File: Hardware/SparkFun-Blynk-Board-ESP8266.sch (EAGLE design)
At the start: 104 parts, among them IC1 LMV358, Q1 2.5A/30V, Q2 MMBT2222A, Q3 MMBT2222A, U1 MCP73831, U2 ESP8266, U3 AP2112K-3.3V, U4 FT231XS-U, U5 W25Q32FVSS, U6 SI7021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

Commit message: Moving some silk. Updating version number to v10.
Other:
- note added: "v10"
- note removed: "v02"
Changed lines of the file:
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@@
 <grid distance="0.1" unitdist="inch" unit="inch" style="lines" multiple="1" display="no" altdistance="0.01" altunitdist="inch" altunit="inch"/>
 <layers>
-<layer number="1" name="Top" color="4" fill="1" visible="yes" active="no"/>
-<layer number="2" name="Route2" color="1" fill="3" visible="yes" active="no"/>
-<layer number="3" name="Route3" color="4" fill="3" visible="yes" active="no"/>
-<layer number="4" name="Route4" color="1" fill="4" visible="yes" active="no"/>
-<layer number="5" name="Route5" color="4" fill="4" visible="yes" active="no"/>
-<layer number="6" name="Route6" color="1" fill="8" visible="yes" active="no"/>
-<layer number="7" name="Route7" color="4" fill="8" visible="yes" active="no"/>
-<layer number="8" name="Route8" color="1" fill="2" visible="yes" active="no"/>
-<layer number="9" name="Route9" color="4" fill="2" visible="yes" active="no"/>
-<layer number="10" name="Route10" color="1" fill="7" visible="yes" active="no"/>
-<layer number="11" name="Route11" color="4" fill="7" visible="yes" active="no"/>
-<layer number="12" name="Route12" color="1" fill="5" visible="yes" active="no"/>
-<layer number="13" name="Route13" color="4" fill="5" visible="yes" active="no"/>
-<layer number="14" name="Route14" color="1" fill="6" visible="yes" active="no"/>
-<layer number="15" name="Route15" color="4" fill="6" visible="yes" active="no"/>
-<layer number="16" name="Bottom" color="1" fill="1" visible="yes" active="no"/>
-<layer number="17" name="Pads" color="2" fill="1" visible="yes" active="no"/>
-<layer number="18" name="Vias" color="2" fill="1" visible="yes" active="no"/>
-<layer number="19" name="Unrouted" color="6" fill="1" visible="yes" active="no"/>
-<layer number="20" name="Dimension" color="15" fill="1" visible="yes" active="no"/>
-<layer number="21" name="tPlace" color="16" fill="1" visible="yes" active="no"/>
-<layer number="22" name="bPlace" color="14" fill="1" visible="yes" active="no"/>
-<layer number="23" name="tOrigins" color="15" fill="1" visible="yes" active="no"/>
-<layer number="24" name="bOrigins" color="15" fill="1" visible="yes" active="no"/>
-<layer number="25" name="tNames" color="7" fill="1" visible="yes" active="no"/>
-<layer number="26" name="bNames" color="7" fill="1" visible="yes" active="no"/>
-<layer number="27" name="tValues" color="7" fill="1" visible="yes" active="no"/>
-<layer number="28" name="bValues" color="7" fill="1" visible="yes" active="no"/>
+<layer number="1" name="Top" color="4" fill="1" visible="no" active="no"/>
+<layer number="2" name="Route2" color="1" fill="3" visible="no" active="no"/>
+<layer number="3" name="Route3" color="4" fill="3" visible="no" active="no"/>
+<layer number="4" name="Route4" color="1" fill="4" visible="no" active="no"/>
+<layer number="5" name="Route5" color="4" fill="4" visible="no" active="no"/>
+<layer number="6" name="Route6" color="1" fill="8" visible="no" active="no"/>
+<layer number="7" name="Route7" color="4" fill="8" visible="no" active="no"/>
+<layer number="8" name="Route8" color="1" fill="2" visible="no" active="no"/>
+<layer number="9" name="Route9" color="4" fill="2" visible="no" active="no"/>
+<layer number="10" name="Route10" color="1" fill="7" visible="no" active="no"/>
+<layer number="11" name="Route11" color="4" fill="7" visible="no" active="no"/>
+<layer number="12" name="Route12" color="1" fill="5" visible="no" active="no"/>
+<layer number="13" name="Route13" color="4" fill="5" visible="no" active="no"/>
+<layer number="14" name="Route14" color="1" fill="6" visible="no" active="no"/>
+<layer number="15" name="Route15" color="4" fill="6" visible="no" active="no"/>
+<layer number="16" name="Bottom" color="1" fill="1" visible="no" active="no"/>
+<layer number="17" name="Pads" color="2" fill="1" visible="no" active="no"/>
+<layer number="18" name="Vias" color="2" fill="1" visible="no" active="no"/>
+<layer number="19" name="Unrouted" color="6" fill="1" visible="no" active="no"/>
+<layer number="20" name="Dimension" color="15" fill="1" visible="no" active="no"/>
+<layer number="21" name="tPlace" color="16" fill="1" visible="no" active="no"/>
+<layer number="22" name="bPlace" color="14" fill="1" visible="no" active="no"/>
+<layer number="23" name="tOrigins" color="15" fill="1" visible="no" active="no"/>
+<layer number="24" name="bOrigins" color="15" fill="1" visible="no" active="no"/>
+<layer number="25" name="tNames" color="7" fill="1" visible="no" active="no"/>
+<layer number="26" name="bNames" color="7" fill="1" visible="no" active="no"/>
+<layer number="27" name="tValues" color="7" fill="1" visible="no" active="no"/>
+<layer number="28" name="bValues" color="7" fill="1" visible="no" active="no"/>
 <layer number="29" name="tStop" color="7" fill="3" visible="no" active="no"/>
 <layer number="30" name="bStop" color="7" fill="6" visible="no" active="no"/>
@@
 <layer number="35" name="tGlue" color="7" fill="4" visible="no" active="no"/>
 <layer number="36" name="bGlue" color="7" fill="5" visible="no" active="no"/>
-<layer number="37" name="tTest" color="7" fill="1" visible="yes" active="no"/>
-<layer number="38" name="bTest" color="7" fill="1" visible="yes" active="no"/>
+<layer number="37" name="tTest" color="7" fill="1" visible="no" active="no"/>
+<layer number="38" name="bTest" color="7" fill="1" visible="no" active="no"/>
 <layer number="39" name="tKeepout" color="4" fill="11" visible="no" active="no"/>
 <layer number="40" name="bKeepout" color="1" fill="11" visible="no" active="no"/>
@@
 <layer number="44" name="Drills" color="7" fill="1" visible="no" active="no"/>
 <layer number="45" name="Holes" color="7" fill="1" visible="no" active="no"/>
-<layer number="46" name="Milling" color="3" fill="1" visible="yes" active="no"/>
-<layer number="47" name="Measures" color="7" fill="1" visible="yes" active="no"/>
-<layer number="48" name="Document" color="7" fill="1" visible="yes" active="no"/>
-<layer number="49" name="Reference" color="7" fill="1" visible="yes" active="no"/>
-<layer number="50" name="dxf" color="7" fill="1" visible="yes" active="no"/>
-<layer number="51" name="tDocu" color="6" fill="1" visible="yes" active="no"/>
-<layer number="52" name="bDocu" color="7" fill="1" visible="yes" active="no"/>
-<layer number="53" name="tGND_GNDA" color="7" fill="9" visible="yes" active="no"/>
-<layer number="54" name="bGND_GNDA" color="1" fill="9" visible="yes" active="no"/>
-<layer number="56" name="wert" color="7" fill="1" visible="yes" active="no"/>
-<layer number="57" name="tCAD" color="7" fill="1" visible="yes" active="no"/>
-<layer number="59" name="tCarbon" color="7" fill="1" visible="yes" active="no"/>
-<layer number="60" name="bCarbon" color="7" fill="1" visible="yes" active="no"/>
+<layer number="46" name="Milling" color="3" fill="1" visible="no" active="no"/>
+<layer number="47" name="Measures" color="7" fill="1" visible="no" active="no"/>
+<layer number="48" name="Document" color="7" fill="1" visible="no" active="no"/>
+<layer number="49" name="Reference" color="7" fill="1" visible="no" active="no"/>
+<layer number="50" name="dxf" color="7" fill="1" visible="no" active="no"/>
+<layer number="51" name="tDocu" color="6" fill="1" visible="no" active="no"/>
+<layer number="52" name="bDocu" color="7" fill="1" visible="no" active="no"/>
+<layer number="53" name="tGND_GNDA" color="7" fill="9" visible="no" active="no"/>
+<layer number="54" name="bGND_GNDA" color="1" fill="9" visible="no" active="no"/>
+<layer number="56" name="wert" color="7" fill="1" visible="no" active="no"/>
+<layer number="57" name="tCAD" color="7" fill="1" visible="no" active="no"/>
+<layer number="59" name="tCarbon" color="7" fill="1" visible="no" active="no"/>
+<layer number="60" name="bCarbon" color="7" fill="1" visible="no" active="no"/>
 <layer number="90" name="Modules" color="5" fill="1" visible="yes" active="yes"/>
 <layer number="91" name="Nets" color="2" fill="1" visible="yes" active="yes"/>
@@
 lots of power.)</text>
 <text x="355.346" y="11.43" size="2.54" layer="94" rot="MR180" align="top-left">Jim Lindblom</text>
-<text x="421.64" y="10.16" size="2.54" layer="94" align="top-left">v02</text>
+<text x="421.64" y="10.16" size="2.54" layer="94" align="top-left">v10</text>
 <text x="332.486" y="6.35" size="2.032" layer="97" rot="MR180" align="top-left">Auto-reset circuit based on NodeMCU Dev Kit</text>
 <text x="386.08" y="76.2" size="1.524" layer="97">GPIO2 pulled up in I2C section</text>

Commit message: Updating PROD_ID on JP29.
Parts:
- JP29: PROD_ID TBD -> (none)
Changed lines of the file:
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@@
 <part name="SUPPLY1" library="SparkFun-Aesthetics" deviceset="VCC" device=""/>
 <part name="GND6" library="SparkFun-Aesthetics" deviceset="GND" device=""/>
-<part name="JP29" library="SparkFun-Connectors" deviceset="M04" device="JST-PTH-VERT">
-<attribute name="PROD_ID" value="TBD"/>
-</part>
+<part name="JP29" library="SparkFun-Connectors" deviceset="M04" device="JST-PTH-VERT"/>
 <part name="SUPPLY3" library="SparkFun-Aesthetics" deviceset="VCC" device=""/>
 <part name="GND42" library="SparkFun-Aesthetics" deviceset="GND" device=""/>
@@
 <instance part="JP6" gate="G$1" x="165.1" y="81.28"/>
 <instance part="D4" gate="G$1" x="121.92" y="160.02" rot="MR0"/>
-<instance part="JP14" gate="G$1" x="149.86" y="160.02" smashed="yes" rot="R180">
+<instance part="JP14" gate="J$1" x="149.86" y="160.02" smashed="yes" rot="R180">
 <attribute name="VALUE" x="152.4" y="167.64" size="1.778" layer="96" rot="R180"/>
 <attribute name="NAME" x="152.4" y="154.178" size="1.778" layer="95" rot="R180"/>
@@
 <pinref part="GND25" gate="1" pin="GND"/>
 <wire x1="139.7" y1="160.02" x2="139.7" y2="154.94" width="0.1524" layer="91"/>
-<pinref part="JP14" gate="G$1" pin="2"/>
+<pinref part="JP14" gate="J$1" pin="2"/>
 <wire x1="142.24" y1="160.02" x2="139.7" y2="160.02" width="0.1524" layer="91"/>
 </segment>
@@
 <segment>
 <pinref part="D4" gate="G$1" pin="DOUT"/>
-<pinref part="JP14" gate="G$1" pin="3"/>
+<pinref part="JP14" gate="J$1" pin="3"/>
 <wire x1="127" y1="157.48" x2="142.24" y2="157.48" width="0.1524" layer="91"/>
 </segment>
@@
 <net name="N$19" class="0">
 <segment>
-<pinref part="JP14" gate="G$1" pin="1"/>
+<pinref part="JP14" gate="J$1" pin="1"/>
 <wire x1="142.24" y1="162.56" x2="139.7" y2="162.56" width="0.1524" layer="91"/>
 <pinref part="SJ3" gate="G$1" pin="1"/>

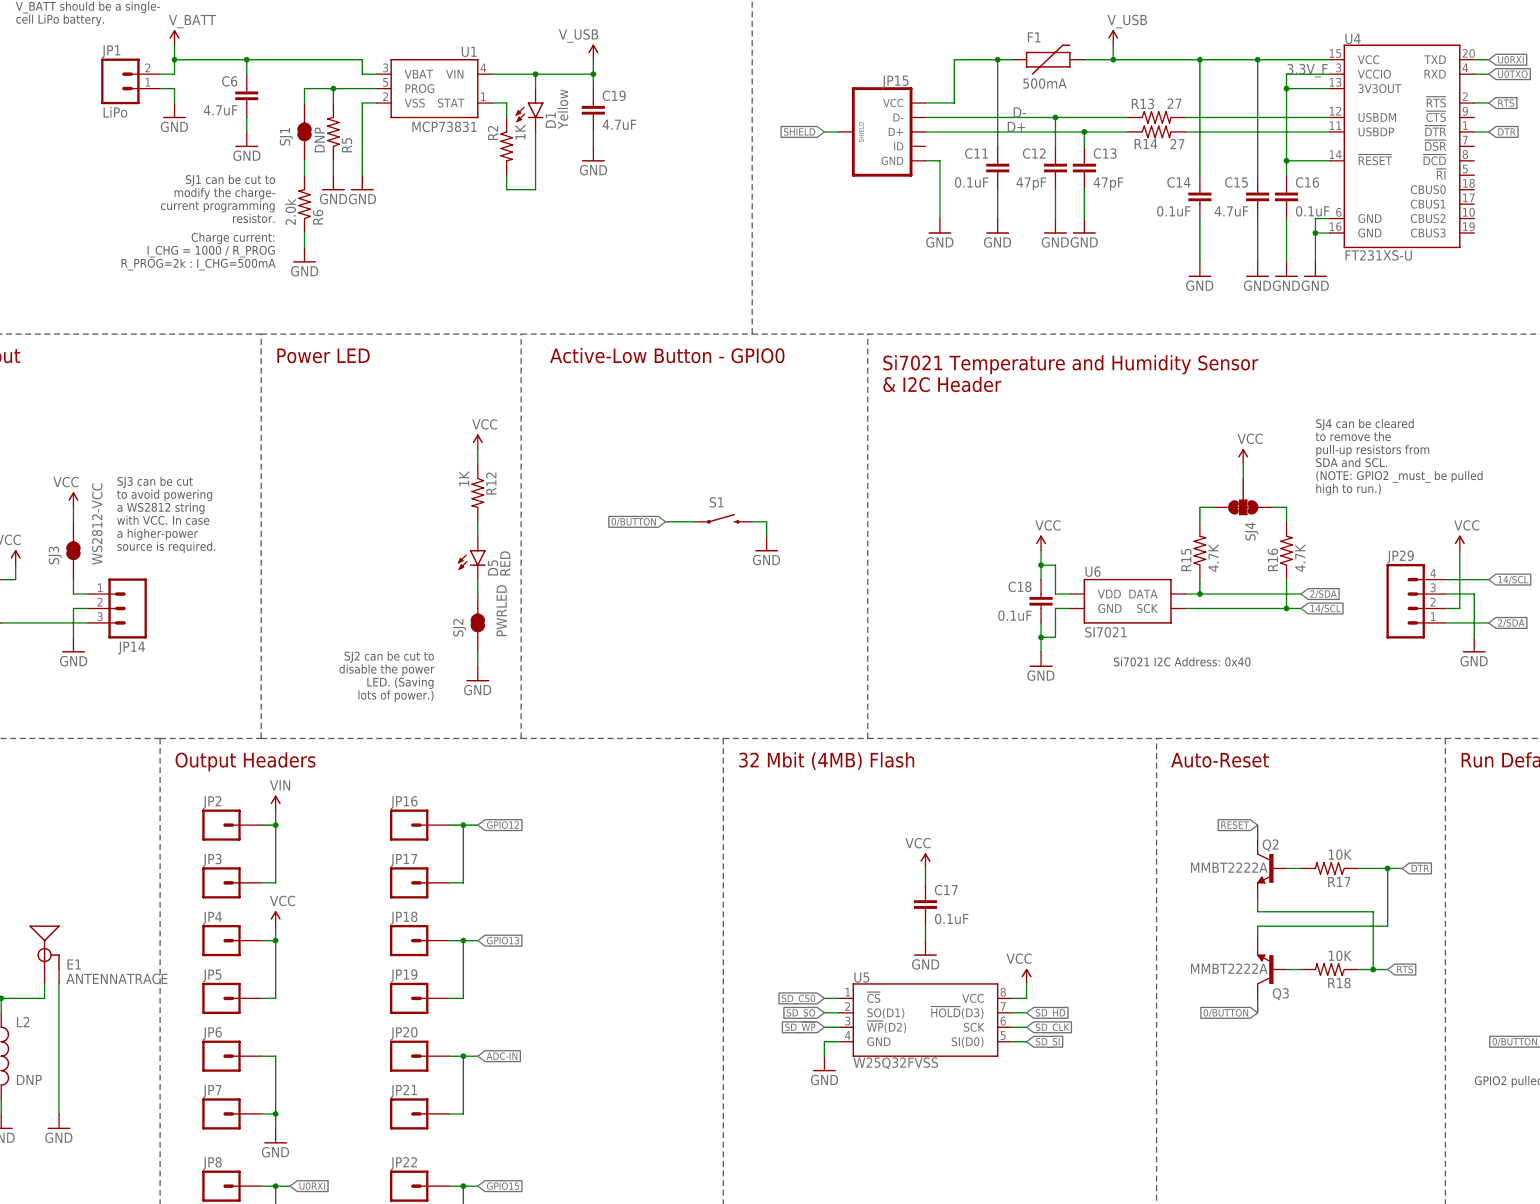
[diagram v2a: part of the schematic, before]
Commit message: Adding values to all parts
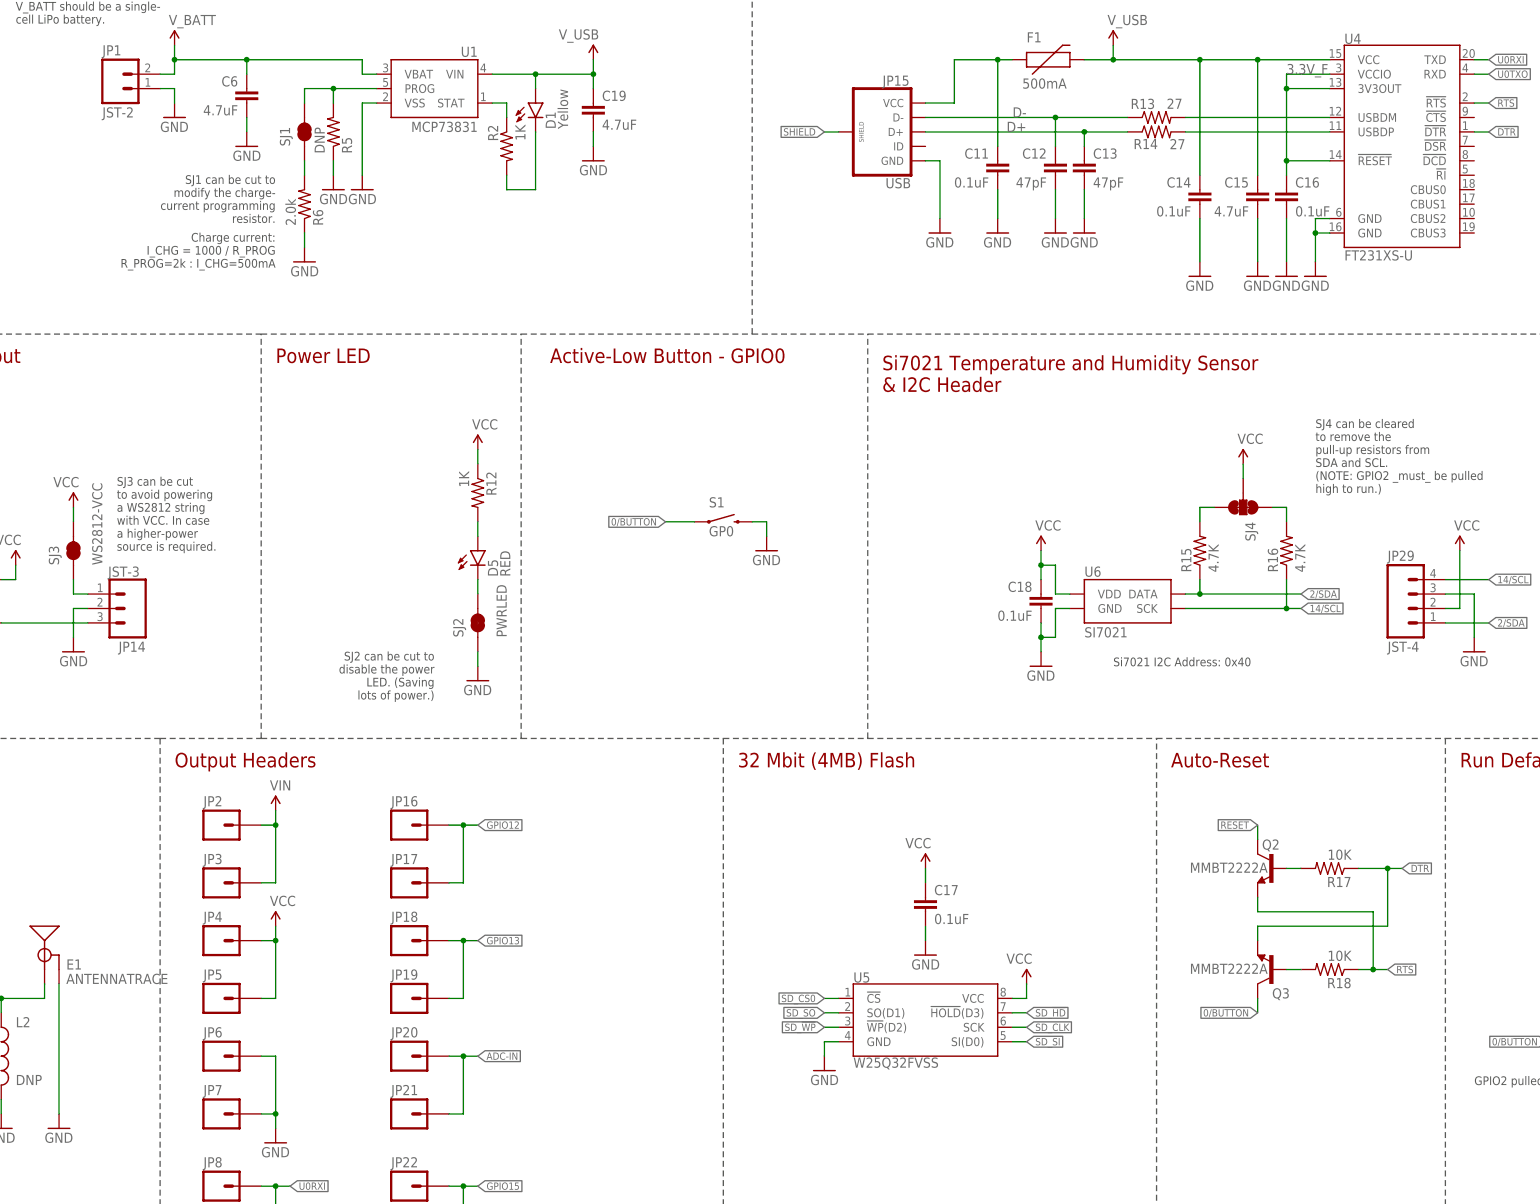
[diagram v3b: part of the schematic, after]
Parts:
- JP1: value LiPo -> JST-2
- JP10, JP12, JP16, JP18, JP2, JP20, JP22, JP24, JP26, JP4, JP6, JP8: value M01ALLIGATOR_HALF -> DNP
- JP11, JP13, JP17, JP19, JP21, JP23, JP25, JP27, JP28, JP3, JP30, JP5, JP7, JP9, SJ4: value (none) -> DNP
- JP14: value (none) -> JST-3
- JP15: value (none) -> USB
- JP29: value (none) -> JST-4
- S1: value SWITCH-MOMENTARY-2SMD-REDUNDANT -> GP0
- SJ1: value JUMPER-PAD-2-NC_BY_TRACE -> DNP

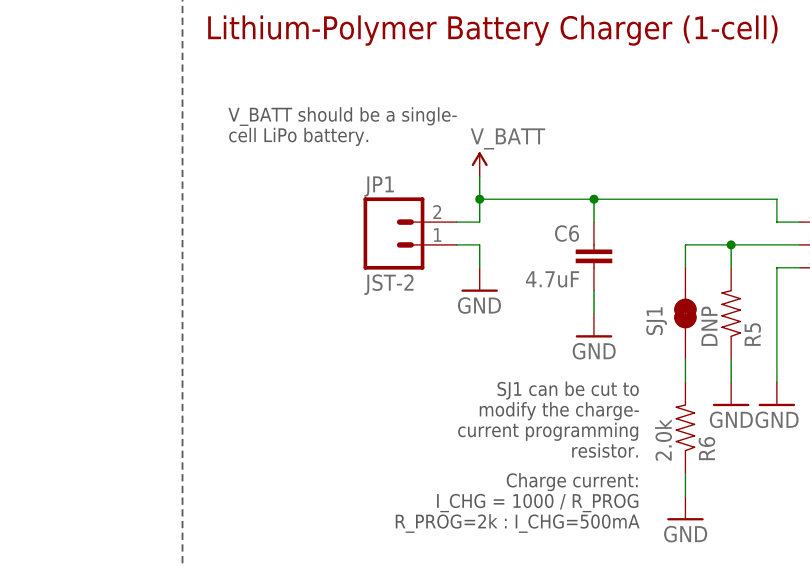
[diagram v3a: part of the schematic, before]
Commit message: Adding value to 2-pin JST
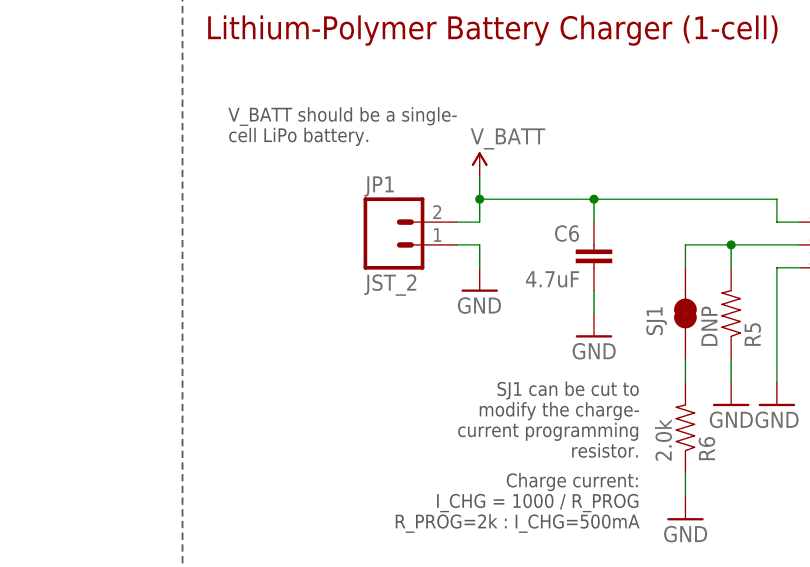
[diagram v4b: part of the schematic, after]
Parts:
- JP1: value JST-2 -> JST_2
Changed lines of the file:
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@@
 <part name="GND13" library="SparkFun-Aesthetics" deviceset="GND" device=""/>
 <part name="SUPPLY7" library="SparkFun-Aesthetics" deviceset="VIN" device=""/>
-<part name="JP1" library="SparkFun-Connectors" deviceset="M02" device="JST-PTH-2" value="JST-2"/>
+<part name="JP1" library="SparkFun-Connectors" deviceset="M02" device="JST-PTH-2" value="JST_2"/>
 <part name="GND4" library="SparkFun-Aesthetics" deviceset="GND" device=""/>
 <part name="D1" library="SparkFun-LED" deviceset="LED-YELLOW" device="0603" value="Yellow"/>
